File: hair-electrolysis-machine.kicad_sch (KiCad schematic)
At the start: 4 parts

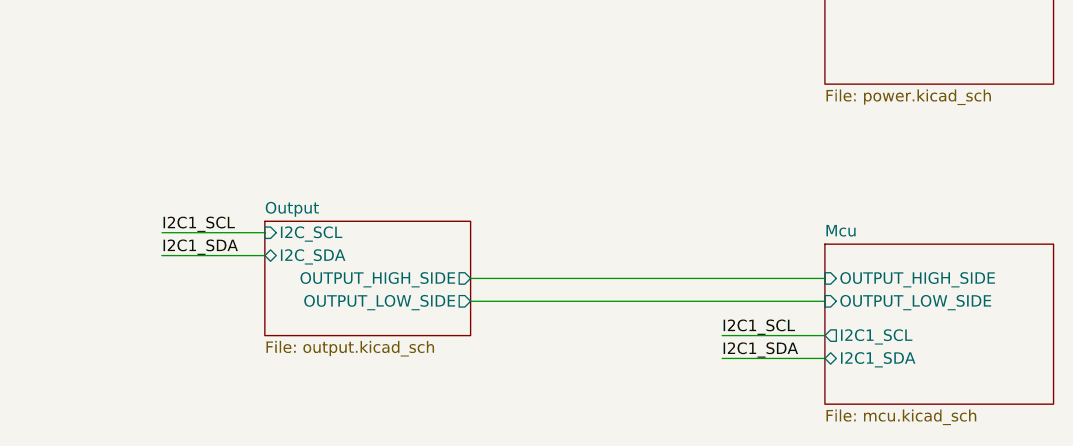
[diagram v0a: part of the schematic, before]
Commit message: Beginning of redesign to use STM32G0B1RETx
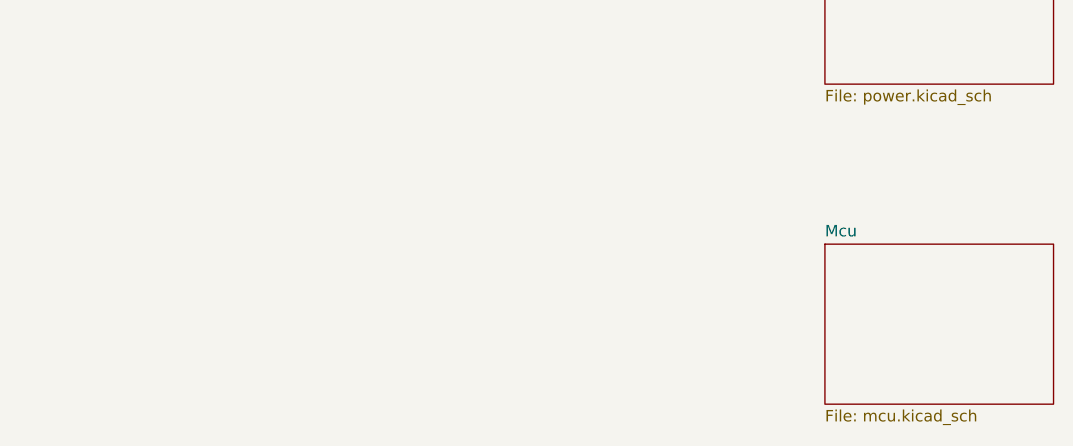
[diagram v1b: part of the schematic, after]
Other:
- removed sheet Output
- sheet Mcu ports: added none; removed I2C1_SCL, I2C1_SDA, OUTPUT_HIGH_SIDE, OUTPUT_LOW_SIDE
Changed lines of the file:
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@@
-	(wire
-		(pts
-			(xy 154.94 69.85) (xy 166.37 69.85)
-		)
-		(stroke
-			(width 0)
-			(type default)
-		)
-	)
 	(wire
 		(pts
@@
 	(wire
 		(pts
-			(xy 189.23 74.93) (xy 228.6 74.93)
-		)
-		(stroke
-			(width 0)
-			(type default)
-		)
-	)
-	(wire
-		(pts
 			(xy 27.94 30.48) (xy 30.48 30.48)
-		)
-		(stroke
-			(width 0)
-			(type default)
-		)
-	)
-	(wire
-		(pts
-			(xy 189.23 72.39) (xy 228.6 72.39)
-		)
-		(stroke
-			(width 0)
-			(type default)
-		)
-	)
-	(wire
-		(pts
-			(xy 217.17 78.74) (xy 228.6 78.74)
-		)
-		(stroke
-			(width 0)
-			(type default)
-		)
-	)
-	(wire
-		(pts
-			(xy 217.17 81.28) (xy 228.6 81.28)
 		)
 		(stroke
@@
 			(width 0)
 			(type default)
-		)
-	)
-	(wire
-		(pts
-			(xy 154.94 67.31) (xy 166.37 67.31)
-		)
-		(stroke
-			(width 0)
-			(type default)
-		)
-	)
-	(label "I2C1_SDA"
-		(at 217.17 81.28 0)
-		(effects
-			(font
-				(size 1.27 1.27)
-			)
-			(justify left bottom)
-		)
-	)
-	(label "I2C1_SDA"
-		(at 154.94 69.85 0)
-		(effects
-			(font
-				(size 1.27 1.27)
-			)
-			(justify left bottom)
-		)
-	)
-	(label "I2C1_SCL"
-		(at 154.94 67.31 0)
-		(effects
-			(font
-				(size 1.27 1.27)
-			)
-			(justify left bottom)
-		)
-	)
-	(label "I2C1_SCL"
-		(at 217.17 78.74 0)
-		(effects
-			(font
-				(size 1.27 1.27)
-			)
-			(justify left bottom)
 		)
 	)
@@
 			)
 		)
-		(pin "OUTPUT_HIGH_SIDE" input
-			(at 228.6 72.39 180)
-			(effects
-				(font
-					(size 1.27 1.27)
-				)
-				(justify left)
-			)
-		)
-		(pin "OUTPUT_LOW_SIDE" input
-			(at 228.6 74.93 180)
-			(effects
-				(font
-					(size 1.27 1.27)
-				)
-				(justify left)
-			)
-		)
-		(pin "I2C1_SCL" output
-			(at 228.6 78.74 180)
-			(effects
-				(font
-					(size 1.27 1.27)
-				)
-				(justify left)
-			)
-		)
-		(pin "I2C1_SDA" bidirectional
-			(at 228.6 81.28 180)
-			(effects
-				(font
-					(size 1.27 1.27)
-				)
-				(justify left)
-			)
-		)
 		(instances
 			(project "hair-electrolysis-machine"
@@
 				)
 			)
-		)
-	)
-	(sheet
-		(at 166.37 66.04)
-		(size 22.86 12.7)
-		(exclude_from_sim no)
-		(in_bom yes)
-		(on_board yes)
-		(dnp no)
-		(fields_autoplaced yes)
-		(stroke
-			(width 0.1524)
-			(type solid)
-		)
-		(fill
-			(color 0 0 0 0.0000)
-		)
-		(property "Sheetname" "Output"
-			(at 166.37 65.3284 0)
-			(effects
-				(font
-					(size 1.27 1.27)
-				)
-				(justify left bottom)
-			)
-		)
-		(property "Sheetfile" "output.kicad_sch"
-			(at 166.37 79.3246 0)
-			(effects
-				(font
-					(size 1.27 1.27)
-				)
-				(justify left top)
-			)
-		)
-		(pin "OUTPUT_HIGH_SIDE" output
-			(at 189.23 72.39 0)
-			(effects
-				(font
-					(size 1.27 1.27)
-				)
-				(justify right)
-			)
-		)
-		(pin "OUTPUT_LOW_SIDE" output
-			(at 189.23 74.93 0)
-			(effects
-				(font
-					(size 1.27 1.27)
-				)
-				(justify right)
-			)
-		)
-		(pin "I2C_SCL" input
-			(at 166.37 67.31 180)
-			(effects
-				(font
-					(size 1.27 1.27)
-				)
-				(justify left)
-			)
-		)
-		(pin "I2C_SDA" bidirectional
-			(at 166.37 69.85 180)
-			(effects
-				(font
-					(size 1.27 1.27)
-				)
-				(justify left)
-			)
-		)
-		(instances
-			(project "hair-electrolysis-machine"
-				(path "/724ce5ca-e5bf-4553-b755-84be7690a548"
-					(page "4")
-				)
-			)

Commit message: stm32g0
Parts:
- H1, H2, H3, H4: footprint MountingHole:MountingHole_2.5mm_Pad -> MountingHole:MountingHole_3.2mm_M3
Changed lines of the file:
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@@
 			)
 		)
-		(property "Footprint" "MountingHole:MountingHole_2.5mm_Pad"
+		(property "Footprint" "MountingHole:MountingHole_3.2mm_M3"
 			(at 38.1 27.94 0)
 			(effects
@@
 		(on_board yes)
 		(dnp no)
-		(fields_autoplaced yes)
 		(property "Reference" "H1"
 			(at 25.4 25.4578 0)
@@
 			)
 		)
-		(property "Footprint" "MountingHole:MountingHole_2.5mm_Pad"
+		(property "Footprint" "MountingHole:MountingHole_3.2mm_M3"
 			(at 22.86 27.94 0)
 			(effects
@@
 			)
 		)
-		(property "Footprint" "MountingHole:MountingHole_2.5mm_Pad"
+		(property "Footprint" "MountingHole:MountingHole_3.2mm_M3"
 			(at 33.02 27.94 0)
 			(effects
@@
 			)
 		)
-		(property "Footprint" "MountingHole:MountingHole_2.5mm_Pad"
+		(property "Footprint" "MountingHole:MountingHole_3.2mm_M3"
 			(at 27.94 27.94 0)
 			(effects

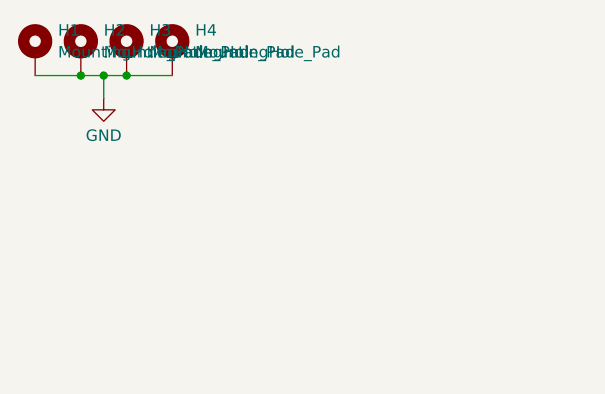
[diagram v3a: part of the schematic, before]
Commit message: Use STM32G0B1RBTx, fix up some silkscreen, maybe production ready?
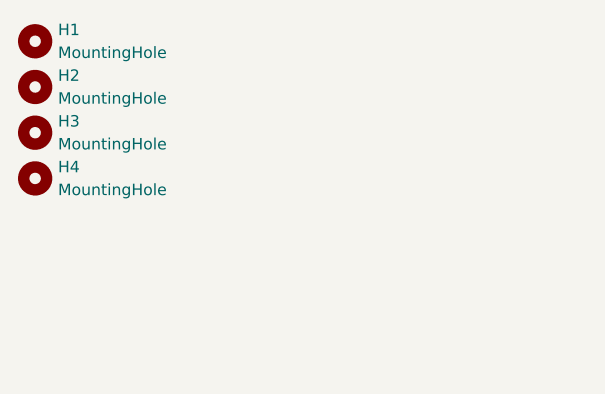
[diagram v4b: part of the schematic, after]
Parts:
- removed H1, H2, H3, H4: MountingHole_Pad, MountingHole:MountingHole_3.2mm_M3, symbol Mechanical:MountingHole_Pad
- added H1, H2, H3, H4: MountingHole, MountingHole:MountingHole_3.2mm_M3, symbol Mechanical:MountingHole

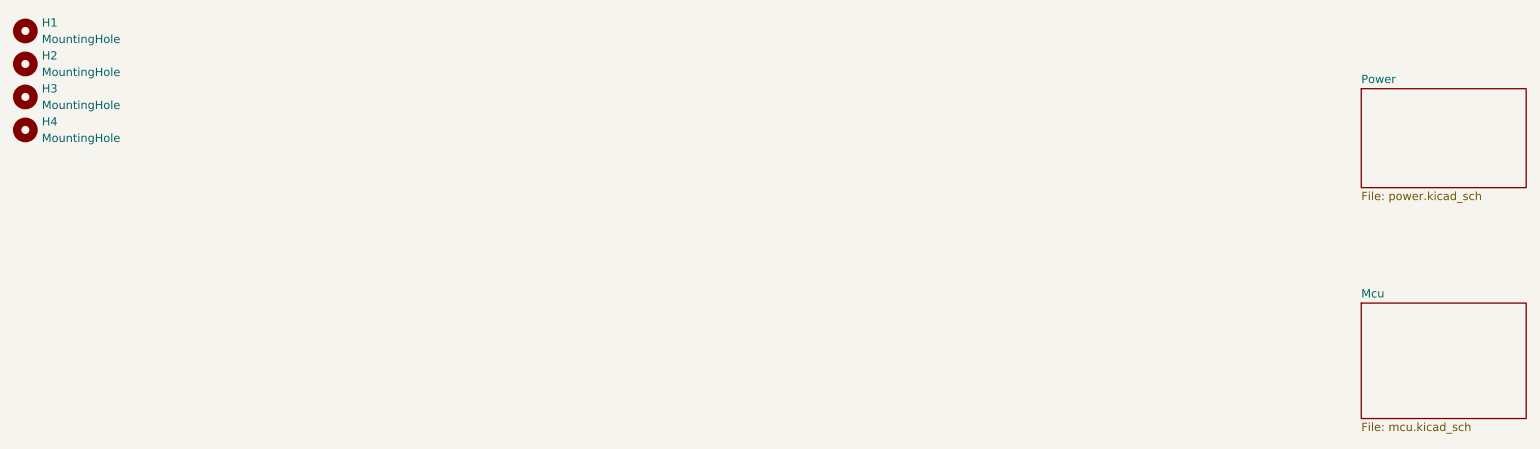
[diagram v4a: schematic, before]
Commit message: Added wire routing hole
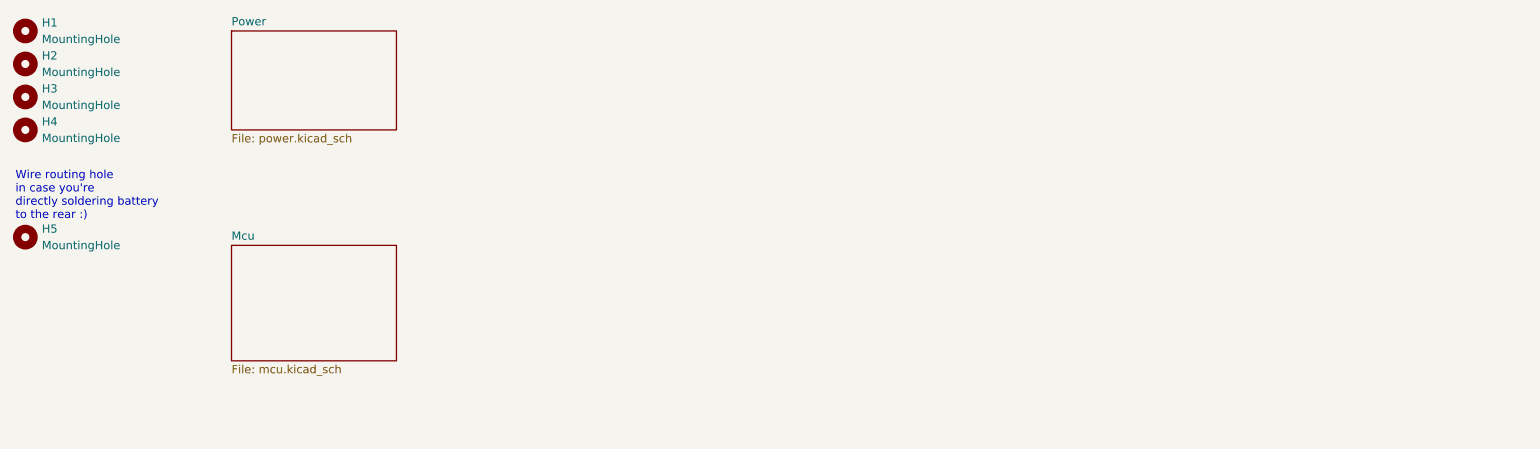
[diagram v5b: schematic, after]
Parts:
- added H5: MountingHole, MountingHole:MountingHole_2.5mm, symbol Mechanical:MountingHole
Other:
- note added: "Wire routing hole in case you're directly soldering battery to the rear :)"
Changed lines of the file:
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@@
 	(generator_version "10.0")
 	(paper "A4")
+	(text "Wire routing hole\nin case you're\ndirectly soldering battery\nto the rear :)"
+		(exclude_from_sim no)
+		(at 21.336 52.07 0)
+		(effects
+			(font
+				(size 1.27 1.27)
+			)
+			(justify left)
+		)
+	)
+	(symbol
+		(lib_id "Mechanical:MountingHole")
+		(at 22.86 58.42 0)
+		(unit 1)
+		(body_style 1)
+		(exclude_from_sim no)
+		(in_bom no)
+		(on_board yes)
+		(in_pos_files yes)
+		(dnp no)
+		(fields_autoplaced yes)
+		(property "Reference" "H5"
+			(at 25.4 57.1499 0)
+			(show_name no)
+			(do_not_autoplace no)
+			(effects
+				(font
+					(size 1.27 1.27)
+				)
+				(justify left)
+			)
+		)
+		(property "Value" "MountingHole"
+			(at 25.4 59.6899 0)
+			(show_name no)
+			(do_not_autoplace no)
+			(effects
+				(font
+					(size 1.27 1.27)
+				)
+				(justify left)
+			)
+		)
+		(property "Footprint" "MountingHole:MountingHole_2.5mm"
+			(at 22.86 58.42 0)
+			(hide yes)
+			(show_name no)
+			(do_not_autoplace no)
+			(effects
+				(font
+					(size 1.27 1.27)
+				)
+			)
+		)
+		(property "Datasheet" ""
+			(at 22.86 58.42 0)
+			(hide yes)
+			(show_name no)
+			(do_not_autoplace no)
+			(effects
+				(font
+					(size 1.27 1.27)
+				)
+			)
+		)
+		(property "Description" "Mounting Hole without connection"
+			(at 22.86 58.42 0)
+			(hide yes)
+			(show_name no)
+			(do_not_autoplace no)
+			(effects
+				(font
+					(size 1.27 1.27)
+				)
+			)
+		)
+		(instances
+			(project "hair-electrolysis-machine"
+				(path "/724ce5ca-e5bf-4553-b755-84be7690a548"
+					(reference "H5")
+					(unit 1)
+				)
+			)
+		)
+	)
 	(symbol
 		(lib_id "Mechanical:MountingHole")
@@
 	)
 	(sheet
-		(at 228.6 35.56)
+		(at 54.61 26.67)
 		(size 25.4 15.24)
 		(exclude_from_sim no)
@@
 		)
 		(property "Sheetname" "Power"
-			(at 228.6 34.8484 0)
+			(at 54.61 25.9584 0)
 			(show_name no)
 			(do_not_autoplace no)
@@
 		)
 		(property "Sheetfile" "power.kicad_sch"
-			(at 228.6 51.3846 0)
+			(at 54.61 42.4946 0)
 			(show_name no)
 			(do_not_autoplace no)
@@
 	)
 	(sheet
-		(at 228.6 68.58)
+		(at 54.61 59.69)
 		(size 25.4 17.78)
 		(exclude_from_sim no)
@@
 		)
 		(property "Sheetname" "Mcu"
-			(at 228.6 67.8684 0)
+			(at 54.61 58.9784 0)
 			(show_name no)
 			(do_not_autoplace no)
@@
 		)
 		(property "Sheetfile" "mcu.kicad_sch"
-			(at 228.6 86.9446 0)
-			(show_name no)
-			(do_not_autoplace no)
+			(at 54.61 78.0546 0)
+			(show_name no)
+			(do_not_autoplace no)
